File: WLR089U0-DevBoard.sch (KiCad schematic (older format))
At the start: 27 parts, among them IC1 WLR089U0-I_RM, J1 USB_B_Micro, J2 Conn_ARM_JTAG_SWD_10, J3 Conn_01x10_Female, J4 Conn_01x02_Male, J5 Conn_01x10_Female, J6 Conn_01x08_Male, SW1 SW_Push, U1 MCP1700-3302E_SOT23, U2 CH304E

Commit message: coupling cap placement pending
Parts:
- C3, C4, C5: footprint Capacitor_SMD:C_0402_1005Metric_Pad0.74x0.62mm_HandSolder -> Capacitor_SMD:C_1206_3216Metric_Pad1.33x1.80mm_HandSolder
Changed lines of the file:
@@
 F 0 "C3" V 9354 3045 50  0000 C CNN
 F 1 "100n" V 9263 3045 50  0000 C CNN
-F 2 "Capacitor_SMD:C_0402_1005Metric_Pad0.74x0.62mm_HandSolder" H 9125 3045 50  0001 C CNN
+F 2 "Capacitor_SMD:C_1206_3216Metric_Pad1.33x1.80mm_HandSolder" H 9125 3045 50  0001 C CNN
 F 3 "~" H 9125 3045 50  0001 C CNN
 	1    9125 3045
@@
 F 0 "C5" V 2270 3090 50  0000 C CNN
 F 1 "100n" V 2200 3095 50  0000 C CNN
-F 2 "Capacitor_SMD:C_0402_1005Metric_Pad0.74x0.62mm_HandSolder" H 2110 3090 50  0001 C CNN
+F 2 "Capacitor_SMD:C_1206_3216Metric_Pad1.33x1.80mm_HandSolder" H 2110 3090 50  0001 C CNN
 F 3 "~" H 2110 3090 50  0001 C CNN
 	1    2110 3090
@@
 F 0 "C4" V 1765 3115 50  0000 C CNN
 F 1 "100n" V 1840 3115 50  0000 C CNN
-F 2 "Capacitor_SMD:C_0402_1005Metric_Pad0.74x0.62mm_HandSolder" H 1945 3105 50  0001 C CNN
+F 2 "Capacitor_SMD:C_1206_3216Metric_Pad1.33x1.80mm_HandSolder" H 1945 3105 50  0001 C CNN
 F 3 "~" H 1945 3105 50  0001 C CNN
 	1    1945 3105

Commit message: Changed orientation, rearranged symbols
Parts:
- JP3: footprint Jumper:SolderJumper-3_P1.3mm_Open_RoundedPad1.0x1.5mm -> Jumper:SolderJumper-2_P1.3mm_Open_RoundedPad1.0x1.5mm
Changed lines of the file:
@@
 EESchema Schematic File Version 4
-LIBS:WLR089U0-DevBoard-cache
 EELAYER 30 0
 EELAYER END
@@
 F 0 "JP3" H 8565 3135 50  0000 C CNN
 F 1 "SolderJumper_2_Open" H 8355 2950 50  0000 C CNN
-F 2 "Jumper:SolderJumper-3_P1.3mm_Open_RoundedPad1.0x1.5mm" H 8565 3045 50  0001 C CNN
+F 2 "Jumper:SolderJumper-2_P1.3mm_Open_RoundedPad1.0x1.5mm" H 8565 3045 50  0001 C CNN
 F 3 "~" H 8565 3045 50  0001 C CNN
 	1    8565 3045

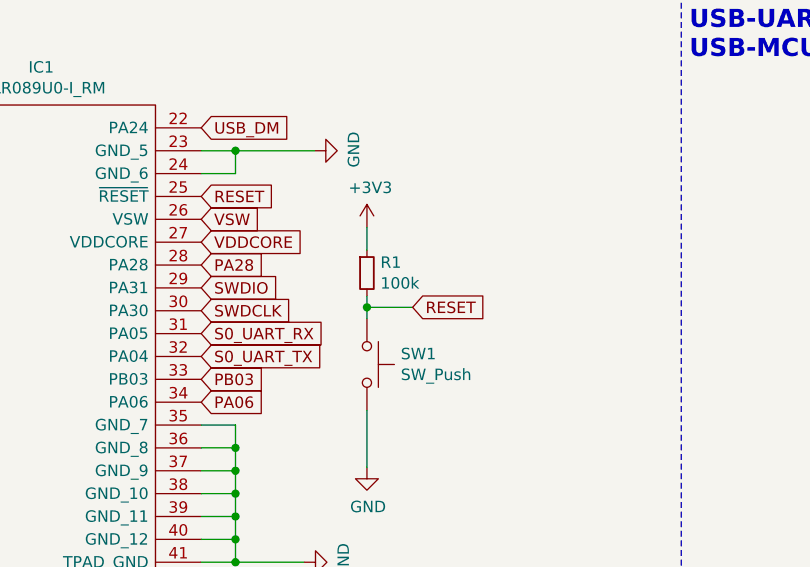
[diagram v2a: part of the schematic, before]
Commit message: Updated bom, chnged 100k to 10k for reset circuit
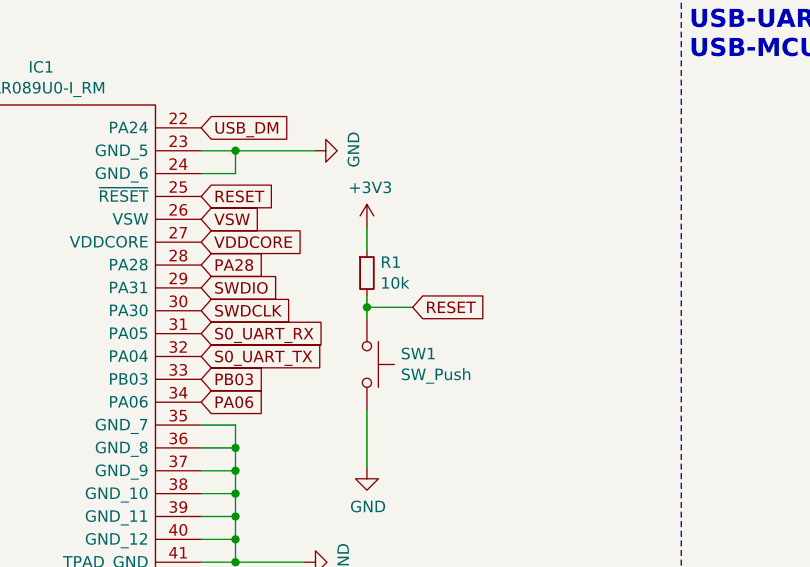
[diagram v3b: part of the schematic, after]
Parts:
- R1: value 100k -> 10k
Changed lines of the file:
@@
 P 4660 3375
 F 0 "R1" H 4719 3421 50  0000 L CNN
-F 1 "100k" H 4719 3330 50  0000 L CNN
+F 1 "10k" H 4719 3330 50  0000 L CNN
 F 2 "Resistor_SMD:R_1206_3216Metric_Pad1.42x1.75mm_HandSolder" H 4660 3375 50  0001 C CNN
 F 3 "~" H 4660 3375 50  0001 C CNN

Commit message: Deleted extra gerber
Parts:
- C1, C2: LCSC (none) -> C412632; Manufacturer_Part_Number (none) -> 1206B105K250CT
- C3, C4, C5: LCSC (none) -> C692631; Manufacturer_Part_Number (none) -> 1206B104K500CT
- D1, D2: LCSC (none) -> C84260; Manufacturer_Part_Number (none) -> RD-LED-0805
- J1: LCSC (none) -> C77238
- J2: LCSC (none) -> C124387
- J3, J5: LCSC (none) -> C57369
- J4: LCSC (none) -> C124375
- J6: LCSC (none) -> C124381
- R1: LCSC (none) -> C17902
- R2, R3: LCSC (none) -> C1469
- R4, R5: LCSC (none) -> C104821
- SW1: LCSC (none) -> C455280
- U1: LCSC (none) -> C39051
- U2: LCSC (none) -> C99652
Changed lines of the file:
@@
 F 2 "Capacitor_SMD:C_1206_3216Metric_Pad1.33x1.80mm_HandSolder" H 2610 1370 50  0001 C CNN
 F 3 "~" H 2610 1370 50  0001 C CNN
+F 4 "1206B105K250CT" H 2610 1370 50  0001 C CNN "Manufacturer_Part_Number"
+F 5 "C412632	" H 2610 1370 50  0001 C CNN "LCSC"
 	1    2610 1370
 	1    0    0    -1
@@
 F 2 "Capacitor_SMD:C_1206_3216Metric_Pad1.33x1.80mm_HandSolder" H 4010 1380 50  0001 C CNN
 F 3 "~" H 4010 1380 50  0001 C CNN
+F 4 "1206B105K250CT" H 4010 1380 50  0001 C CNN "Manufacturer_Part_Number"
+F 5 "C412632	" H 4010 1380 50  0001 C CNN "LCSC"
 	1    4010 1380
 	1    0    0    -1
@@
 F 2 "Resistor_SMD:R_1206_3216Metric_Pad1.42x1.75mm_HandSolder" H 6790 1445 50  0001 C CNN
 F 3 "~" H 6790 1445 50  0001 C CNN
+F 4 "C1469" H 6790 1445 50  0001 C CNN "LCSC"
 	1    6790 1445
 	0    1    1    0
@@
 F 2 "LED_SMD:LED_0805_2012Metric_Pad1.15x1.40mm_HandSolder" V 7925 1425 50  0001 C CNN
 F 3 "~" V 7925 1425 50  0001 C CNN
+F 4 "RD-LED-0805" H 7925 1425 50  0001 C CNN "Manufacturer_Part_Number"
+F 5 "C84260" H 7925 1425 50  0001 C CNN "LCSC"
 	1    7925 1425
 	-1   0    0    1
@@
 F 2 "Resistor_SMD:R_1206_3216Metric_Pad1.42x1.75mm_HandSolder" H 8260 1425 50  0001 C CNN
 F 3 "~" H 8260 1425 50  0001 C CNN
+F 4 "C1469" H 8260 1425 50  0001 C CNN "LCSC"
 	1    8260 1425
 	0    1    1    0
@@
 F 2 "Capacitor_SMD:C_1206_3216Metric_Pad1.33x1.80mm_HandSolder" H 9125 3045 50  0001 C CNN
 F 3 "~" H 9125 3045 50  0001 C CNN
+F 4 "1206B104K500CT" H 9125 3045 50  0001 C CNN "Manufacturer_Part_Number"
+F 5 "C692631" H 9125 3045 50  0001 C CNN "LCSC"
 	1    9125 3045
 	0    -1   -1   0
@@
 F 2 "Package_TO_SOT_SMD:SOT-23" H 3325 1335 50  0001 C CNN
 F 3 "http://ww1.microchip.com/downloads/en/DeviceDoc/20001826D.pdf" H 3325 1110 50  0001 C CNN
+F 4 "C39051" H 3325 1110 50  0000 C CNN "LCSC"
 	1    3325 1110
 	1    0    0    -1
@@
 F 2 "WLR089u0-DevBoard:Tactile Switch 3x4x2mm" H 4660 3975 50  0001 C CNN
 F 3 "~" H 4660 3975 50  0001 C CNN
+F 4 "C455280" H 4660 3775 50  0001 C CNN "LCSC"
 	1    4660 3775
 	0    1    1    0
@@
 F 2 "Resistor_SMD:R_1206_3216Metric_Pad1.42x1.75mm_HandSolder" H 4660 3375 50  0001 C CNN
 F 3 "~" H 4660 3375 50  0001 C CNN
+F 4 "C17902" H 4660 3375 50  0001 C CNN "LCSC"
 	1    4660 3375
 	1    0    0    -1
@@
 F 2 "Connector_USB:USB_Micro-AB_Molex_47590-0001" H 1230 1225 50  0001 C CNN
 F 3 "~" H 1230 1225 50  0001 C CNN
+F 4 "C77238" H 1080 1275 50  0000 C CNN "LCSC"
 	1    1080 1275
 	1    0    0    -1
@@
 F 2 "Connector_PinHeader_1.27mm:PinHeader_2x05_P1.27mm_Vertical" H 1650 6585 50  0001 C CNN
 F 3 "http://infocenter.arm.com/help/topic/com.arm.doc.ddi0314h/DDI0314H_coresight_components_trm.pdf" V 1300 5335 50  0001 C CNN
+F 4 "C124387" H 1650 6585 50  0001 C CNN "LCSC"
 	1    1650 6585
 	1    0    0    -1
@@
 F 2 "Package_SO:MSOP-10_3x3mm_P0.5mm" H 8770 3740 50  0001 C CNN
 F 3 "" H 8770 3740 50  0001 C CNN
+F 4 "C99652" H 8870 3490 50  0001 C CNN "LCSC"
 	1    8870 3490
 	1    0    0    -1
@@
 F 2 "Connector_PinHeader_2.54mm:PinHeader_1x10_P2.54mm_Vertical" H 4455 6290 50  0001 C CNN
 F 3 "~" H 4455 6290 50  0001 C CNN
+F 4 "C57369" H 4455 6290 50  0001 C CNN "LCSC"
 	1    4455 6290
 	1    0    0    -1
@@
 F 2 "Connector_PinHeader_2.54mm:PinHeader_1x10_P2.54mm_Vertical" H 5330 6400 50  0001 C CNN
 F 3 "~" H 5330 6400 50  0001 C CNN
+F 4 "C57369" H 5330 6400 50  0001 C CNN "LCSC"
 	1    5330 6400
 	-1   0    0    1
@@
 F 2 "Connector_PinHeader_2.54mm:PinHeader_1x02_P2.54mm_Vertical" H 5275 1490 50  0001 C CNN
 F 3 "~" H 5275 1490 50  0001 C CNN
+F 4 "C124375" H 5275 1490 50  0001 C CNN "LCSC"
 	1    5275 1490
 	0    -1   -1   0
@@
 F 2 "LED_SMD:LED_0805_2012Metric_Pad1.15x1.40mm_HandSolder" V 6545 1445 50  0001 C CNN
 F 3 "~" V 6545 1445 50  0001 C CNN
+F 4 "RD-LED-0805" H 6545 1445 50  0001 C CNN "Manufacturer_Part_Number"
+F 5 "C84260" H 6545 1445 50  0001 C CNN "LCSC"
 	1    6545 1445
 	-1   0    0    1
@@
 F 2 "Connector_PinHeader_2.54mm:PinHeader_1x08_P2.54mm_Vertical" H 8895 6195 50  0001 C CNN
 F 3 "~" H 8895 6195 50  0001 C CNN
+F 4 "C124381" H 8895 6195 50  0001 C CNN "LCSC"
 	1    8895 6195
 	0    -1   -1   0
@@
 F 2 "Capacitor_SMD:C_1206_3216Metric_Pad1.33x1.80mm_HandSolder" H 2110 3090 50  0001 C CNN
 F 3 "~" H 2110 3090 50  0001 C CNN
+F 4 "1206B104K500CT" H 2110 3090 50  0001 C CNN "Manufacturer_Part_Number"
+F 5 "C692631" H 2110 3090 50  0001 C CNN "LCSC"
 	1    2110 3090
 	1    0    0    -1
@@
 F 2 "Capacitor_SMD:C_1206_3216Metric_Pad1.33x1.80mm_HandSolder" H 1945 3105 50  0001 C CNN
 F 3 "~" H 1945 3105 50  0001 C CNN
+F 4 "1206B104K500CT" H 1945 3105 50  0001 C CNN "Manufacturer_Part_Number"
+F 5 "C692631" H 1945 3105 50  0001 C CNN "LCSC"
 	1    1945 3105
 	1    0    0    -1
@@
 Wire Wire Line
 	2110 2940 2480 2940
+$Comp
+L power:GND #PWR0102
+U 1 1 602924A9
+P 2110 3190
+F 0 "#PWR0102" H 2110 2940 50  0001 C CNN
+F 1 "GND" H 2115 3017 50  0000 C CNN
+F 2 "" H 2110 3190 50  0001 C CNN
+F 3 "" H 2110 3190 50  0001 C CNN
+	1    2110 3190
+	1    0    0    -1
+$EndComp
+Wire Wire Line
+	1270 3415 1355 3415
+Wire Wire Line
+	2535 3415 2535 3440
+Wire Wire Line
+	1275 3570 1535 3570
+Wire Wire Line
+	2535 3570 2535 3540
+$Comp
+L Device:R_Small R4
+U 1 1 602A5151
+P 1355 3110
+F 0 "R4" H 1195 3145 50  0000 L CNN
+F 1 "4.7k" H 1110 3070 50  0000 L CNN
+F 2 "Resistor_SMD:R_1206_3216Metric_Pad1.42x1.75mm_HandSolder" H 1355 3110 50  0001 C CNN
+F 3 "~" H 1355 3110 50  0001 C CNN
+F 4 "C104821" H 1355 3110 50  0001 C CNN "LCSC"
+	1    1355 3110
+	1    0    0    -1
+$EndComp
+$Comp
+L Device:R_Small R5
+U 1 1 602A607E
+P 1535 3115
+F 0 "R5" H 1594 3161 50  0000 L CNN
+F 1 "4.7k" H 1594 3070 50  0000 L CNN
+F 2 "Resistor_SMD:R_1206_3216Metric_Pad1.42x1.75mm_HandSolder" H 1535 3115 50  0001 C CNN
+F 3 "~" H 1535 3115 50  0001 C CNN
+F 4 "C104821" H 1535 3115 50  0001 C CNN "LCSC"
+	1    1535 3115
+	1    0    0    -1
+$EndComp
+Wire Wire Line
+	1355 3010 1355 2925
+Wire Wire Line
+	1355 2925 1425 2925
+Wire Wire Line
+	1535 3015 1535 2925
+Wire Wire Line
+	1535 2925 1425 2925
+Connection ~ 1425 2925
+Wire Wire Line
+	1355 3210 1355 3415
+Connection ~ 1355 3415
+Wire Wire Line
+	1355 3415 2535 3415
+Wire Wire Line
+	1535 3215 1535 3570
+Connection ~ 1535 3570
+Wire Wire Line
+	1535 3570 2535 3570
+$Comp
+L power:+3V3 #PWR0103
+U 1 1 602BADF9
+P 1865 2665
+F 0 "#PWR0103" H 1865 2515 50  0001 C CNN
+F 1 "+3V3" H 1880 2838 50  0000 C CNN
+F 2 "" H 1865 2665 50  0001 C CNN
+F 3 "" H 1865 2665 50  0001 C CNN
+	1    1865 2665
+	1    0    0    -1
+$EndComp
+Connection ~ 1865 2665
+Wire Wire Line
+	1865 2665 1865 2940
 $Comp
 L power:GND #PWR0101
@@
 	1    0    0    -1
 $EndComp
-$Comp
-L power:GND #PWR0102
-U 1 1 602924A9
-P 2110 3190
-F 0 "#PWR0102" H 2110 2940 50  0001 C CNN
-F 1 "GND" H 2115 3017 50  0000 C CNN
-F 2 "" H 2110 3190 50  0001 C CNN
-F 3 "" H 2110 3190 50  0001 C CNN
-	1    2110 3190
-	1    0    0    -1
-$EndComp
-Wire Wire Line
-	1270 3415 1355 3415
-Wire Wire Line
-	2535 3415 2535 3440
-Wire Wire Line
-	1275 3570 1535 3570
-Wire Wire Line
-	2535 3570 2535 3540
-$Comp
-L Device:R_Small R4
-U 1 1 602A5151
-P 1355 3110
-F 0 "R4" H 1195 3145 50  0000 L CNN
-F 1 "4.7k" H 1110 3070 50  0000 L CNN
-F 2 "Resistor_SMD:R_1206_3216Metric_Pad1.42x1.75mm_HandSolder" H 1355 3110 50  0001 C CNN
-F 3 "~" H 1355 3110 50  0001 C CNN
-	1    1355 3110
-	1    0    0    -1
-$EndComp
-$Comp
-L Device:R_Small R5
-U 1 1 602A607E
-P 1535 3115
-F 0 "R5" H 1594 3161 50  0000 L CNN
-F 1 "4.7k" H 1594 3070 50  0000 L CNN
-F 2 "Resistor_SMD:R_1206_3216Metric_Pad1.42x1.75mm_HandSolder" H 1535 3115 50  0001 C CNN
-F 3 "~" H 1535 3115 50  0001 C CNN
-	1    1535 3115
-	1    0    0    -1
-$EndComp
-Wire Wire Line
-	1355 3010 1355 2925
-Wire Wire Line
-	1355 2925 1425 2925
-Wire Wire Line
-	1535 3015 1535 2925
-Wire Wire Line
-	1535 2925 1425 2925
-Connection ~ 1425 2925
-Wire Wire Line
-	1355 3210 1355 3415
-Connection ~ 1355 3415
-Wire Wire Line
-	1355 3415 2535 3415
-Wire Wire Line
-	1535 3215 1535 3570
-Connection ~ 1535 3570
-Wire Wire Line
-	1535 3570 2535 3570
-$Comp
-L power:+3V3 #PWR0103
-U 1 1 602BADF9
-P 1865 2665
-F 0 "#PWR0103" H 1865 2515 50  0001 C CNN
-F 1 "+3V3" H 1880 2838 50  0000 C CNN
-F 2 "" H 1865 2665 50  0001 C CNN
-F 3 "" H 1865 2665 50  0001 C CNN
-	1    1865 2665
-	1    0    0    -1
-$EndComp
-Connection ~ 1865 2665
-Wire Wire Line
-	1865 2665 1865 2940
 $EndSCHEMATC
